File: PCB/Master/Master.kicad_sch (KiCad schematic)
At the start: 62 parts, among them J1 USB_C_Receptacle_USB2.0_16P, J2 Conn_01x05_Pin, J5 Conn_01x09_Pin, J6 Conn_01x09_Pin, Q2 AO3400A, Q3 AO3400A, SW1 PTS810_SJM_250_SMTR_LFS, SW2 PTS810_SJM_250_SMTR_LFS, U1 ESP32-S3-WROOM-1U, U2 TCA9406DC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

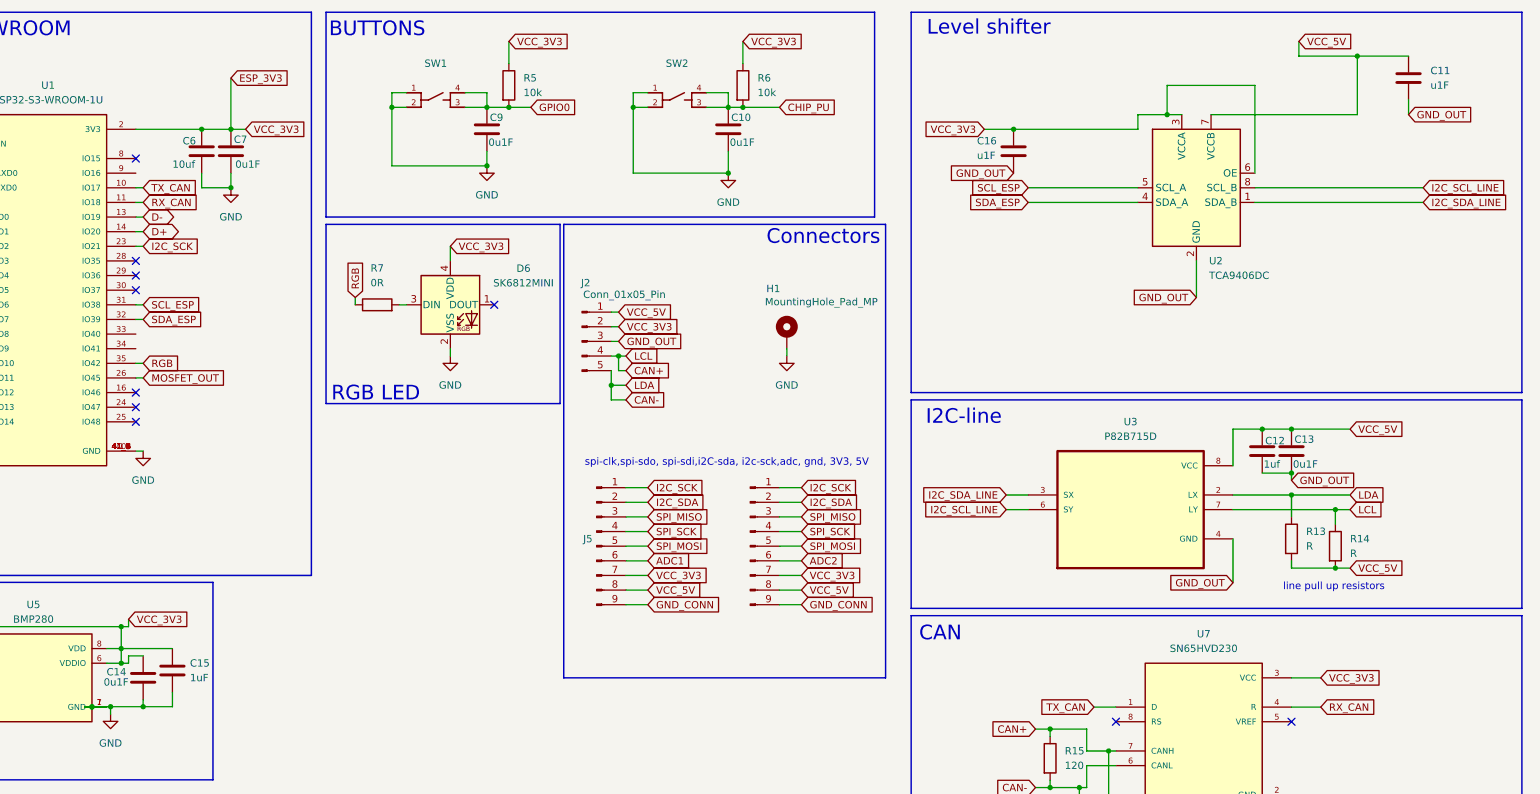
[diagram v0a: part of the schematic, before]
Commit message: Small changes to the pcb(Master and Slave))
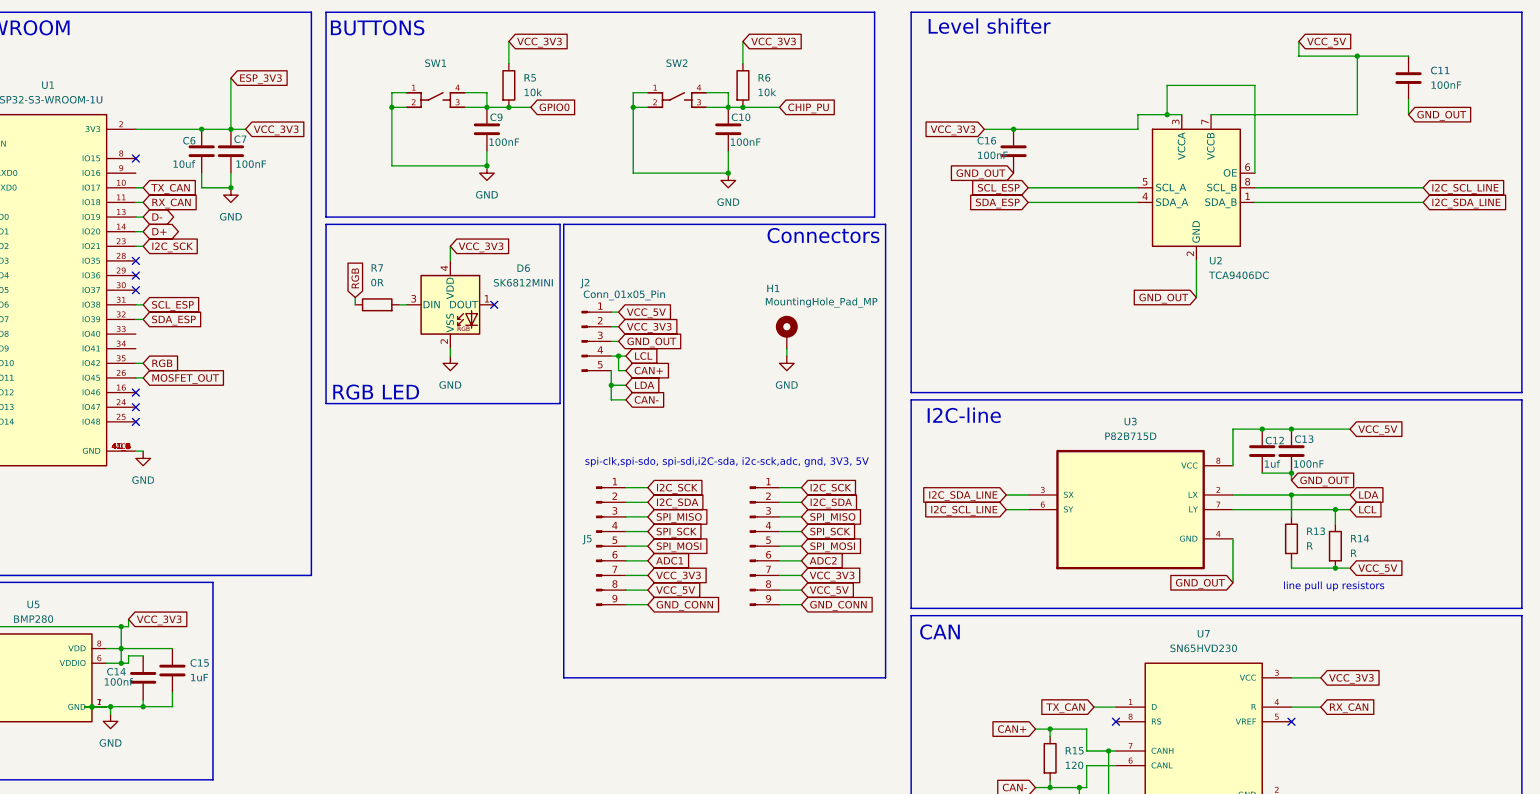
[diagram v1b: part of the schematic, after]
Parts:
- C10, C13, C7, C9: value 0u1F -> 100nF
- C11, C16: value u1F -> 100nF
- C14: value 0u1F -> 100nf
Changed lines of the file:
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@@
 			)
 		)
-		(property "Value" "u1F"
+		(property "Value" "100nF"
 			(at 311.15 45.212 0)
 			(effects
@@
 			)
 		)
-		(property "Value" "u1F"
+		(property "Value" "100nF"
 			(at 389.89 33.0199 0)
 			(effects
@@
 			)
 		)
-		(property "Value" "0u1F"
+		(property "Value" "100nF"
 			(at 226.314 42.926 0)
 			(effects
@@
 			)
 		)
-		(property "Value" "0u1F"
+		(property "Value" "100nF"
 			(at 366.014 98.806 0)
 			(effects
@@
 			)
 		)
-		(property "Value" "0u1F"
+		(property "Value" "100nF"
 			(at 182.372 46.736 0)
 			(effects
@@
 			)
 		)
-		(property "Value" "0u1F"
+		(property "Value" "100nf"
 			(at 159.512 136.652 0)
 			(effects
@@
 			)
 		)
-		(property "Value" "0u1F"
+		(property "Value" "100nF"
 			(at 268.224 42.926 0)
 			(effects

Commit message: Added CAP
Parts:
- added C17: 100nf, Capacitor_SMD:C_0603_1608Metric_Pad1.08x0.95mm_HandSolder, symbol Device:C
- added C22: 1uF, Capacitor_SMD:C_0603_1608Metric_Pad1.08x0.95mm_HandSolder, symbol Device:C
- added C23, C24: 1uf, Capacitor_SMD:C_0603_1608Metric_Pad1.08x0.95mm_HandSolder, symbol Device:C
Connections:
- net ESP_3V3: now also C17.1, C22.1, C24.2
- net GND_OUT: now also C17.2, C22.2, C23.1, C24.1
- net VCC_5V: now also C23.2
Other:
- moved on the sheet: C14, C16

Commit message: From 0603 TO 0805 at power supply
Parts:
- R19, R21: footprint Resistor_SMD:R_0603_1608Metric_Pad0.98x0.95mm_HandSolder -> Resistor_SMD:R_0805_2012Metric_Pad1.20x1.40mm_HandSolder
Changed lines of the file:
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@@
 			)
 		)
-		(property "Footprint" "Resistor_SMD:R_0603_1608Metric_Pad0.98x0.95mm_HandSolder"
+		(property "Footprint" "Resistor_SMD:R_0805_2012Metric_Pad1.20x1.40mm_HandSolder"
 			(at 55.372 106.68 90)
 			(effects
@@
 			)
 		)
-		(property "Footprint" "Resistor_SMD:R_0603_1608Metric_Pad0.98x0.95mm_HandSolder"
+		(property "Footprint" "Resistor_SMD:R_0805_2012Metric_Pad1.20x1.40mm_HandSolder"
 			(at 66.04 104.648 90)
 			(effects

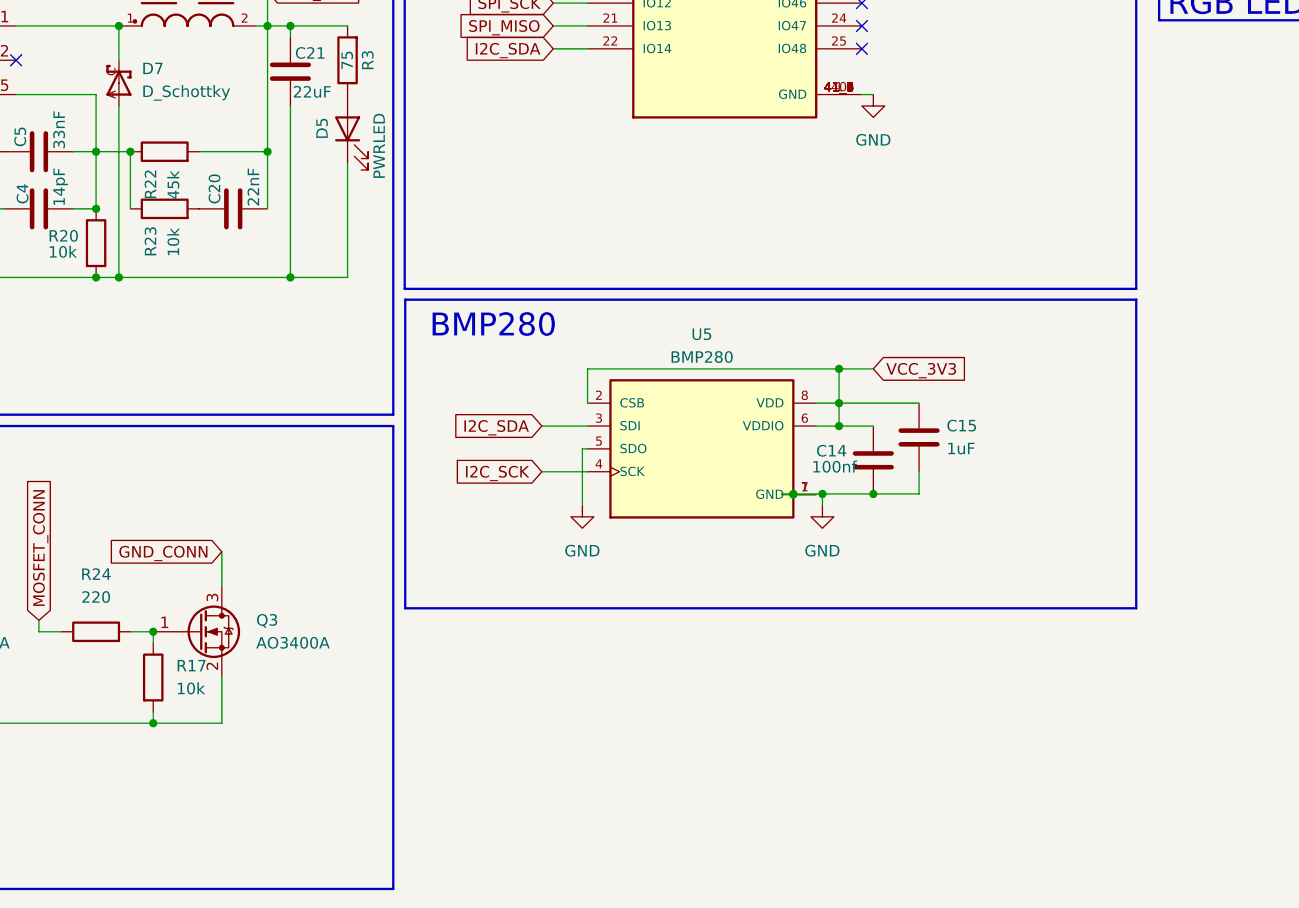
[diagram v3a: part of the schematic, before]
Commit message: Changed bmp for bme
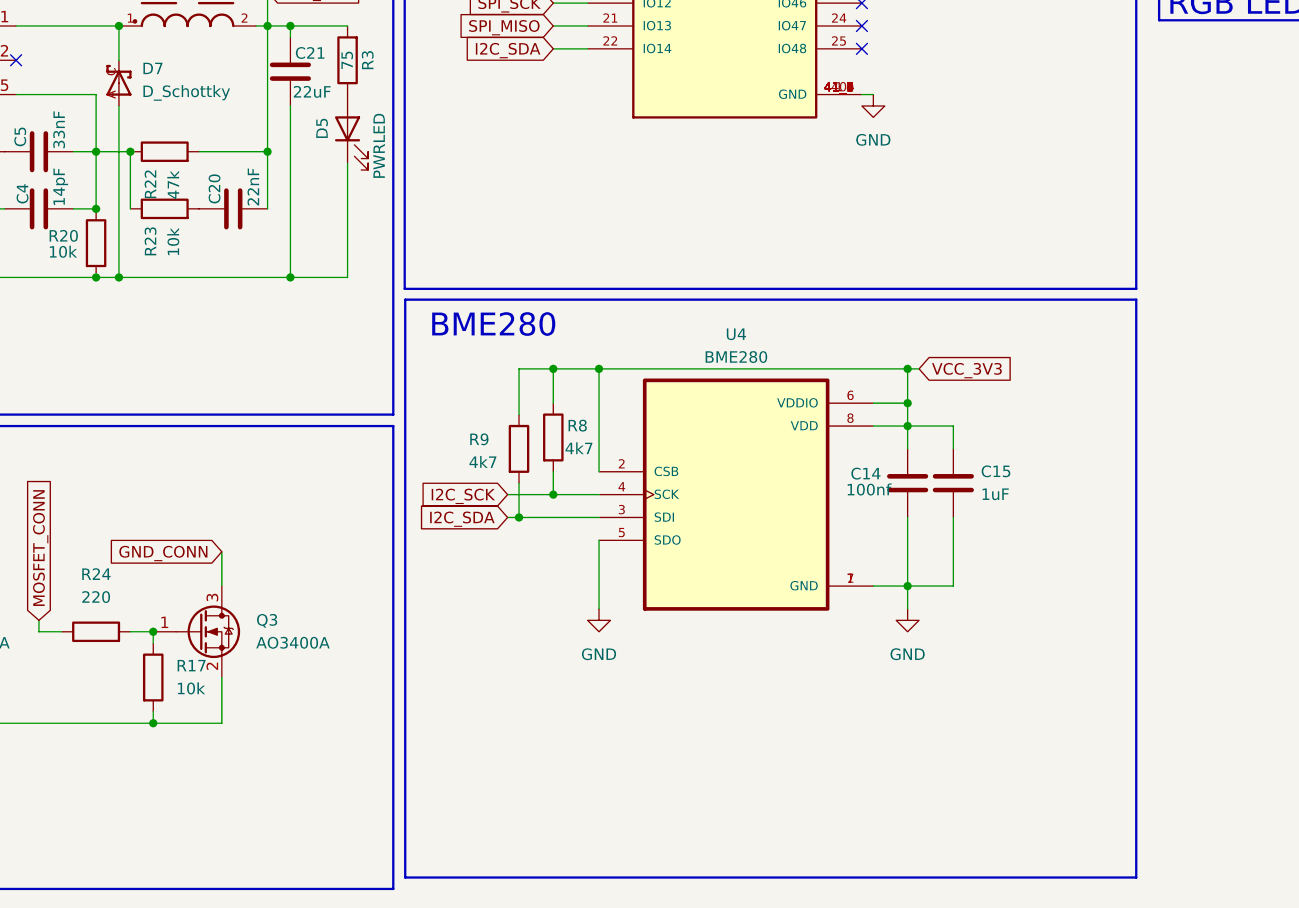
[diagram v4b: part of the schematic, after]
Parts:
- removed U5: BMP280, BMP280:XDCR_BMP280, symbol BMP280:BMP280
- added R8, R9: 4k7, Resistor_SMD:R_0603_1608Metric_Pad0.98x0.95mm_HandSolder, symbol Device:R
- added U4: BME280, BME280:PSON65P250X250X100-8N, symbol BME280:BME280
- R22: value 45k -> 47k
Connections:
- net ESP_3V3: now also R8.1, R9.1, U4.2 (CSB), U4.6 (VDDIO), U4.8 (VDD)
- net GND: now also U4.1 (GND), U4.5 (SDO), U4.7 (GND)
- net I2C_SCK: now also R8.2, U4.4 (SCK)
- net I2C_SDA: now also R9.2, U4.3 (SDI)
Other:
- note added: "BME280"
- note removed: "BMP280"
- moved on the sheet: C14, C15

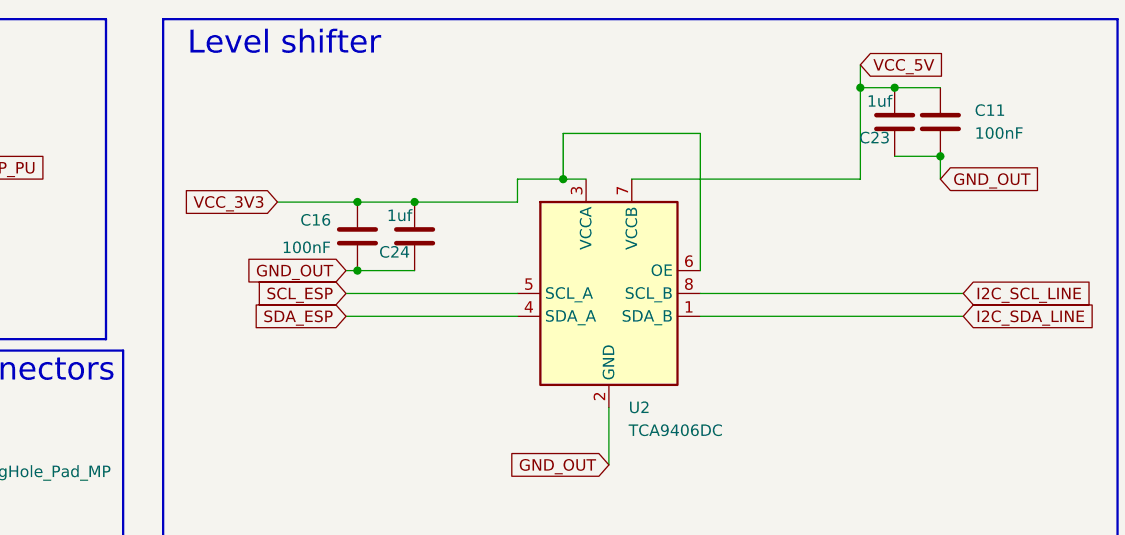
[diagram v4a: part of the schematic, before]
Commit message: Added I2C PullUp Resistors
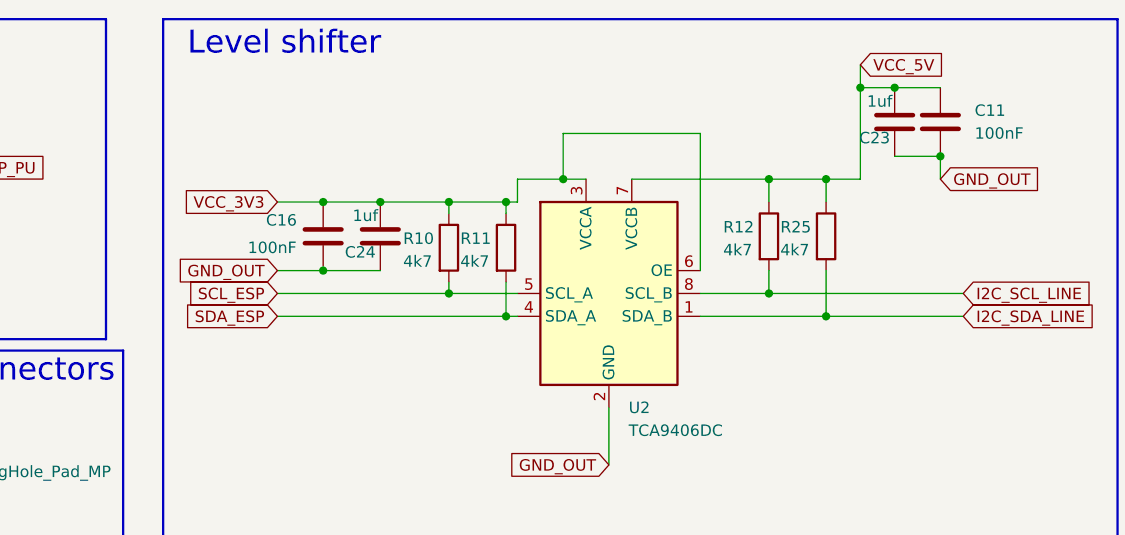
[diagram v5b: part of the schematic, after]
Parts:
- added R10, R11, R12, R25: 4k7, Resistor_SMD:R_0603_1608Metric_Pad0.98x0.95mm_HandSolder, symbol Device:R
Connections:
- net ESP_3V3: now also R10.1, R11.1
- net I2C_SCL_LINE: now also R12.2
- net I2C_SDA_LINE: now also R25.2
- net SCL_ESP: now also R10.2
- net SDA_ESP: now also R11.2
- net VCC_5V: now also R12.1, R25.1
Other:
- moved on the sheet: C16, C24

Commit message: repaired HX711
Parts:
- removed C8: 1uf, Capacitor_SMD:C_0603_1608Metric_Pad1.08x0.95mm_HandSolder, symbol Device:C
- removed R4: 10k, Resistor_SMD:R_0603_1608Metric_Pad0.98x0.95mm_HandSolder, symbol Device:R
- added JP1: SolderJumper_3_Open, Jumper:SolderJumper-3_P1.3mm_Open_RoundedPad1.0x1.5mm, symbol Jumper:SolderJumper_3_Open
- added R26: R, Resistor_SMD:R_0603_1608Metric_Pad0.98x0.95mm_HandSolder, symbol Device:R
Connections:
- net ESP_3V3: now also JP1.3 (B)
- net GND_OUT: now also R26.1
- net CAN_RS: now reaches U7.8 (RS)
- net CAN_RS: now also JP1.2 (C)
- new net: JP1.1 (A), R26.2
- no-connect marks 13 -> 12

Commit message: Update_Prosinec
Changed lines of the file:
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@@
 	(rectangle
 		(start 114.3565 119.3101)
-		(end 195.58 183.515)
+		(end 195.58 184.785)
 		(stroke
 			(width 0.254)

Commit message: SETUP FOR HANDOVER1
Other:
- note added: "BME280/BME680"
- note removed: "BME280"
- title: (none) -> Příloha č.2 schéma QUEEN modulu
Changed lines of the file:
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@@
 	(generator_version "8.0")
 	(paper "A3")
+	(title_block
+		(title "Příloha č.2 schéma QUEEN modulu")
+		(date "2025-28-02")
+		(rev "Lukáš Vágner")
+	)
 	(junction
 		(at 331.47 40.64)
@@
 		)
 	)
-	(text "BME280"
+	(text "BME280/BME680"
 		(exclude_from_sim no)
-		(at 124.1355 122.3581 0)
+		(at 131.318 122.428 0)
 		(effects
 			(font
@@
 		(dnp no)
 		(property "Reference" "C14"
-			(at 163.83 138.684 0)
+			(at 163.068 138.176 0)
 			(effects
 				(font
@@
 		)
 		(property "Value" "100nf"
-			(at 163.322 140.462 0)
+			(at 162.052 140.462 0)
 			(effects
 				(font
